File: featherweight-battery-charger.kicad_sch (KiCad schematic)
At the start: 0 parts

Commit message: page setup and team footprints
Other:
- company: (none) -> Waterloo Rocketry
- title: (none) -> Featherweight Battery Charger
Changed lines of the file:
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@@
 	(generator_version "9.0")
 	(paper "A4")
+	(title_block
+		(title "Featherweight Battery Charger")
+		(date "2025-10-27")
+		(rev "v0")
+		(company "Waterloo Rocketry")
+	)
 	(sheet_instances
 		(path "/"

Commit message: Added components + general layout
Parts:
- added BT1: Battery_Cell, symbol Device:Battery_Cell
- added R1: R, symbol Device:R
- added U1: MCP73832-2-OT, Package_TO_SOT_SMD:SOT-23-5, symbol Battery_Management:MCP73832-2-OT
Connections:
- new net: BT1.2 (-), R1.2, U1.2 (V_{SS})
- new net: BT1.1 (+), U1.4 (V_{DD})
- new net: R1.1, U1.5 (PROG)
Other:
- company: Waterloo Rocketry -> (none)
- title: Featherweight Battery Charger -> (none)

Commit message: updated schematic
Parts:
- removed BT1: Battery_Cell, symbol Device:Battery_Cell
- added BT2: Battery_Cell, symbol Device:Battery_Cell
- added C1, C2: 4.7uF, symbol Device:C_US
- added D1: LED, symbol Device:LED
- added R2: R, symbol Device:R
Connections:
- net at U1.1 (STAT): now also R2.2
- net GND: now reaches R1.2, U1.2 (V_{SS})
- net GND: now also BT2.2 (-), C1.2, C2.2
- net at U1.3 (V_{BAT}): now also BT2.1 (+), C1.1
- net +5V: now reaches U1.4 (V_{DD})
- net +5V: now also C2.1, D1.2 (A)
- new net: D1.1 (K), R2.1

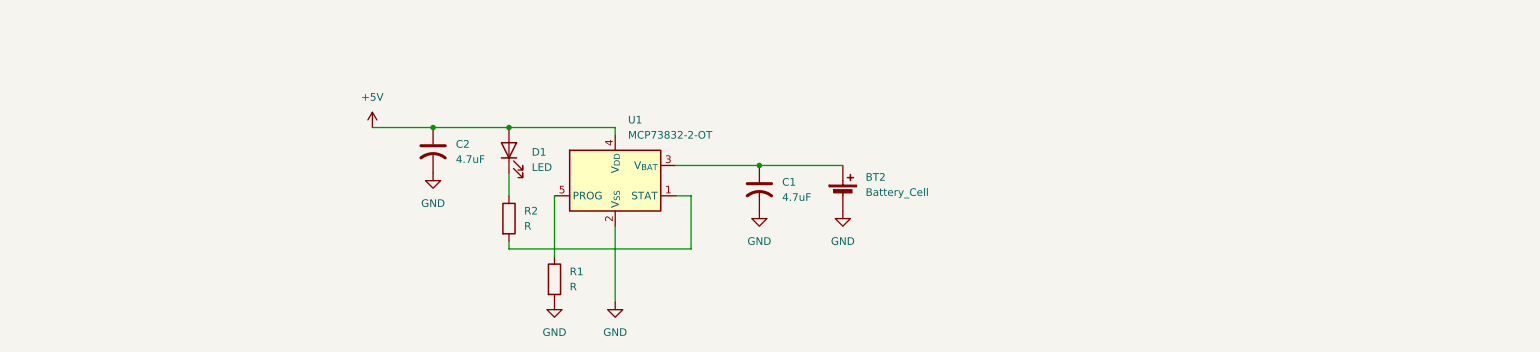
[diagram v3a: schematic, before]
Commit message: buck converter without values
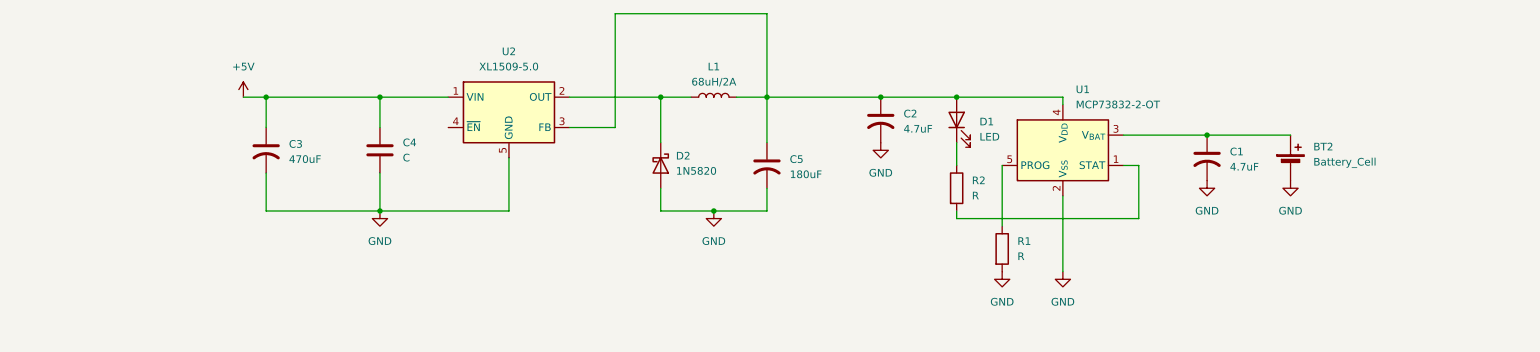
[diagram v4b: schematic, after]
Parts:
- added C3: 470uF, symbol Device:C_US
- added C4: C, symbol Device:C
- added C5: 180uF, symbol Device:C_US
- added D2: 1N5820, Diode_THT:D_DO-201AD_P15.24mm_Horizontal, symbol Diode:1N5820
- added L1: 68uH/2A, symbol Device:L
- added U2: XL1509-5.0, Package_SO:SOIC-8_3.9x4.9mm_P1.27mm, symbol Regulator_Switching:XL1509-5.0
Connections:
- net +5V: now also C3.1, C4.1, U2.1 (VIN); no longer C2.1, D1.2 (A), U1.4 (V_{DD})
- net GND: now also C3.2, C4.2, C5.2, D2.2 (A), U2.5 (GND), U2.6 (GND), U2.7 (GND), U2.8 (GND)
- new net: C2.1, C5.1, D1.2 (A), L1.2, U1.4 (V_{DD}), U2.3 (FB)
- new net: D2.1 (K), L1.1, U2.2 (OUT)
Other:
- moved on the sheet: BT2, C1, C2, D1, R1, R2, U1

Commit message: Changed resistor icon in schematic
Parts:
- R1, R2: symbol Device:R -> Device:R_US
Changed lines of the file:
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@@
 	)
 	(symbol
-		(lib_id "Device:R")
+		(lib_id "Device:R_US")
 		(at 176.53 116.84 0)
 		(unit 1)
@@
 		)
 		(property "Footprint" ""
-			(at 174.752 116.84 90)
+			(at 177.546 117.094 90)
 			(effects
 				(font
@@
 			)
 		)
-		(property "Description" "Resistor"
+		(property "Description" "Resistor, US symbol"
 			(at 176.53 116.84 0)
 			(effects
@@
 	)
 	(symbol
-		(lib_id "Device:R")
+		(lib_id "Device:R_US")
 		(at 184.15 127 0)
 		(unit 1)
@@
 		)
 		(property "Footprint" ""
-			(at 182.372 127 90)
+			(at 185.166 127.254 90)
 			(effects
 				(font
@@
 			)
 		)
-		(property "Description" "Resistor"
+		(property "Description" "Resistor, US symbol"
 			(at 184.15 127 0)
 			(effects

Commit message: finished buck converter part
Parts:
- C4: value C -> 1uF
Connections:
- net +5V renamed +12V
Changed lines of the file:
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@@
+	)
+	(junction
+		(at 144.78 120.65)
+		(diameter 0)
+		(color 0 0 0 0)
 	)
 	(junction
@@
 	(wire
 		(pts
+			(xy 163.83 109.22) (xy 163.83 120.65)
+		)
+		(stroke
+			(width 0)
+			(type default)
+		)
+	)
+	(wire
+		(pts
 			(xy 204.47 107.95) (xy 218.44 107.95)
 		)
@@
 		(pts
 			(xy 101.6 111.76) (xy 101.6 120.65)
+		)
+		(stroke
+			(width 0)
+			(type default)
+		)
+	)
+	(wire
+		(pts
+			(xy 144.78 120.65) (xy 163.83 120.65)
 		)
 		(stroke
@@
 			)
 		)
-		(property "Value" "C"
+		(property "Value" "1uF"
 			(at 83.82 111.7599 0)
 			(effects
@@
 	(symbol
 		(lib_id "power:GND")
-		(at 163.83 109.22 0)
-		(unit 1)
-		(exclude_from_sim no)
-		(in_bom yes)
-		(on_board yes)
-		(dnp no)
-		(fields_autoplaced yes)
-		(property "Reference" "#PWR04"
-			(at 163.83 115.57 0)
-			(effects
-				(font
-					(size 1.27 1.27)
-				)
-				(hide yes)
-			)
-		)
-		(property "Value" "GND"
-			(at 163.83 114.3 0)
-			(effects
-				(font
-					(size 1.27 1.27)
-				)
-			)
-		)
-		(property "Footprint" ""
-			(at 163.83 109.22 0)
-			(effects
-				(font
-					(size 1.27 1.27)
-				)
-				(hide yes)
-			)
-		)
-		(property "Datasheet" ""
-			(at 163.83 109.22 0)
-			(effects
-				(font
-					(size 1.27 1.27)
-				)
-				(hide yes)
-			)
-		)
-		(property "Description" "Power symbol creates a global label with name \"GND\" , ground"
-			(at 163.83 109.22 0)
-			(effects
-				(font
-					(size 1.27 1.27)
-				)
-				(hide yes)
-			)
-		)
-		(pin "1"
-		)
-		(instances
-			(project "featherweight-battery-charger"
-				(path "/5889f758-61b0-4051-8dd5-ccc851807563"
-					(reference "#PWR04")
-					(unit 1)
-				)
-			)
-		)
-	)
-	(symbol
-		(lib_id "power:GND")
 		(at 184.15 130.81 0)
 		(unit 1)
@@
 			)
 		)
-		(property "Value" "+5V"
+		(property "Value" "+12V"
 			(at 57.15 96.52 0)
 			(effects

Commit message: Added resistor values
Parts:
- R1: value R -> 2500
- R2: value R -> 133
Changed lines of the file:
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@@
 			)
 		)
-		(property "Value" "R"
+		(property "Value" "133"
 			(at 179.07 118.1099 0)
 			(effects
@@
 			)
 		)
-		(property "Value" "R"
+		(property "Value" "2500"
 			(at 186.69 128.2699 0)
 			(effects

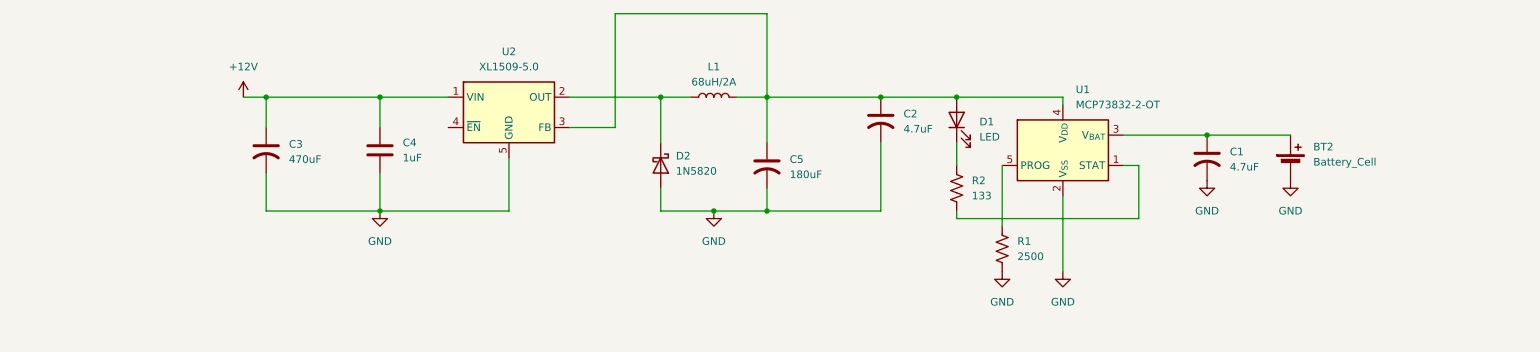
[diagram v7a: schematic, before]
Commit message: Changed Buck, Added Connectors and Fuse
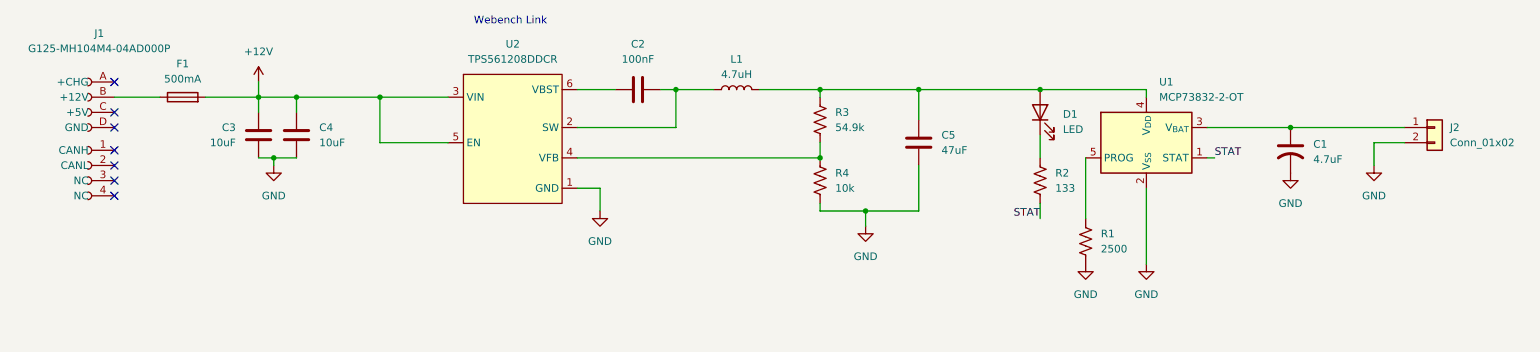
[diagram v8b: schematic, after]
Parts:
- removed BT2: Battery_Cell, symbol Device:Battery_Cell
- removed C2: 4.7uF, symbol Device:C_US
- removed C3: 470uF, symbol Device:C_US
- removed C5: 180uF, symbol Device:C_US
- removed D2: 1N5820, Diode_THT:D_DO-201AD_P15.24mm_Horizontal, symbol Diode:1N5820
- removed U2: XL1509-5.0, Package_SO:SOIC-8_3.9x4.9mm_P1.27mm, symbol Regulator_Switching:XL1509-5.0
- added C2: 100nF, symbol Device:C
- added C3: 10uF, symbol Device:C
- added C5: 47uF, symbol Device:C
- added F1: 500mA, symbol Device:Fuse
- added J1: G125-MH104M4-04AD000P, canhw_footprints:HARWIN_G125-MH104M4-04AD000P, symbol canhw:G125-MH104M4-04AD000P
- added J2: Conn_01x02, symbol Connector_Generic:Conn_01x02
- added R3: 54.9k, symbol Device:R_US
- added R4: 10k, symbol Device:R_US
- added U2: TPS561208DDCR, symbol TPS561208DDCR:TPS561208DDC
- C4: value 1uF -> 10uF
- L1: value 68uH/2A -> 4.7uH
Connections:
- net +12V: now also C4.2, C3.1, F1.2, U2.3 (VIN), U2.5 (EN); no longer C4.1
- net GND: now also C4.1, C3.2, C5.1, J2.2 (Pin_2), R4.1, U2.1 (GND); no longer C4.2
- net at D1.2 (A), L1.2, U1.4 (V_{DD}): now also C5.2, R3.2
- net STAT: now reaches R2.2, U1.1 (STAT)
- net at C1.1, U1.3 (V_{BAT}): now also J2.1 (Pin_1)
- net at L1.1: now also C2.2, U2.2 (SW)
- new net: F1.1, J1.B (+12V)
- new net: R3.1, R4.2, U2.4 (VFB)
- new net: C2.1, U2.6 (VBST)
- no-connect marks 0 -> 7
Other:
- note added: "Webench Link"
- moved on the sheet: C1, D1, R1, R2, U1
